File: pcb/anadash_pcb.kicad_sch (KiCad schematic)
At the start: 32 parts, among them J1 Meter1, J2 Meter2, J3 Meter3, J4 Meter4, SW1 SW_Push, SW2 SW_Push, SW3 SW_Push, SW4 SW_Push, SW5 RotaryEncoder_Switch, SW6 SW_Push, SW7 SW_Push, SW8 SW_Push, SW9 SW_Push, U2 ER_OLEDM0.91_1x-I2C

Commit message: pcb design
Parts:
- removed R5, R6, R7, R8: 330, Resistor_THT:R_Axial_DIN0207_L6.3mm_D2.5mm_P7.62mm_Horizontal, symbol Resistors:Resistor - 1%
- R4: renamed from R1; value 330 -> 680
- R5: renamed from R2; value 330 -> 680
- R6: renamed from R3; value 330 -> 680
- R7: renamed from R4; value 330 -> 680
- TP1: value GND -> GNDTP
- TP2: value 5VTestPoint -> 5VTP
- TP3: value 3V3TestPoint -> 3V3TP
- U2: footprint Display:ER_OLEDM0.91_1x-I2C -> Display:Adafruit_SSD1306
- renumbered R10 to R1, R11 to R2, R9 to R3
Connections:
- net +3V3: now also U1.7 (VCC); no longer U1. (VCC)
- net GND: now also U1.8 (GND); no longer U1. (VCC)
- net SCL: now also U1.9 (SCL); no longer U1. (VCC)
- net SDA: now also U1.10 (SDA); no longer U1. (VCC)
- net at J2.1 (Pin_1): now also R5.2
- net at R6.2: now also J3.1 (Pin_1)
- net at R5.1: now also U1.3 (VB); no longer U1. (VCC)
- net at R4.1: now also U1.2 (VA); no longer U1. (VCC)
- net at R7.1: now also U1.5 (VD); no longer U1. (VCC)
- net at R6.1: now also U1.4 (VC); no longer U1. (VCC)
- net at J4.1 (Pin_1): now also R7.2
- net at J1.1 (Pin_1): now also R4.2
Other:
- moved on the sheet: J1, J2, J3, J4

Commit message: fresh start to pcb
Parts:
- U2: footprint Display:Adafruit_SSD1306 -> Connector_JST:JST_XH_B4B-XH-A_1x04_P2.50mm_Vertical
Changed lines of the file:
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@@
 			)
 		)
-		(property "Footprint" "Display:Adafruit_SSD1306"
+		(property "Footprint" "Connector_JST:JST_XH_B4B-XH-A_1x04_P2.50mm_Vertical"
 			(at 247.904 110.49 0)
 			(hide yes)

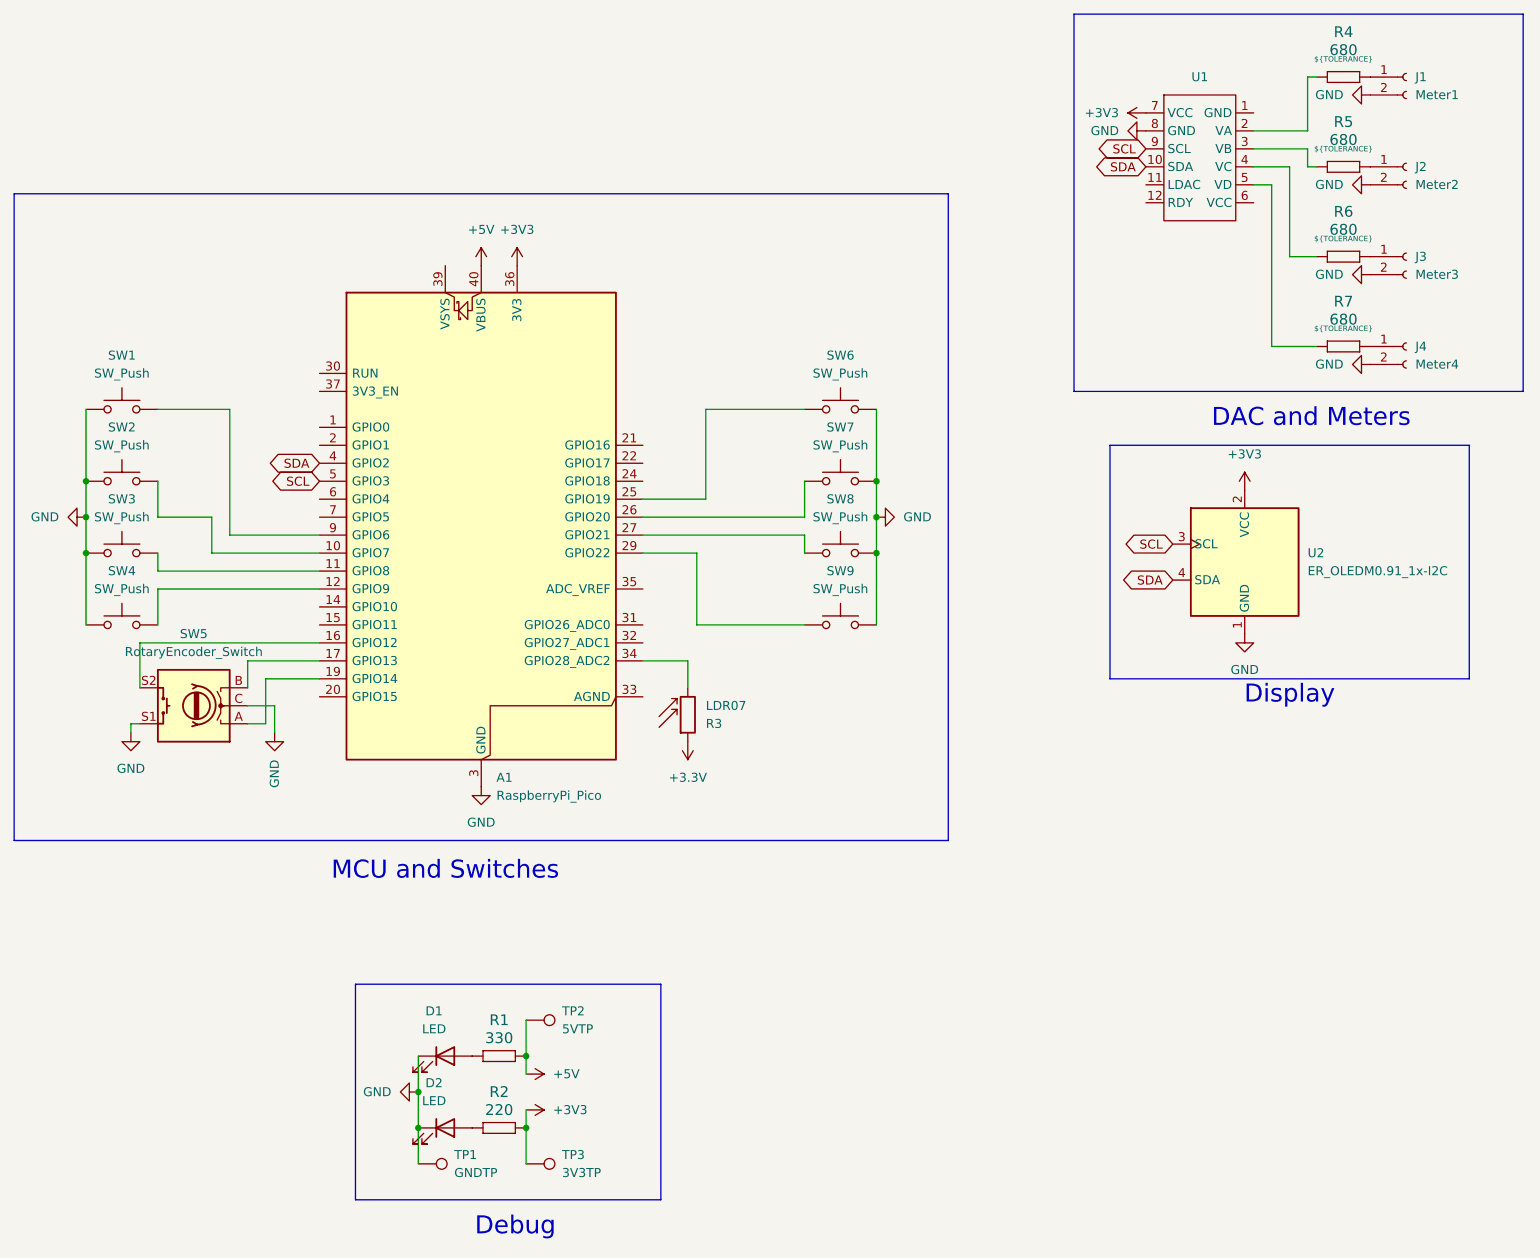
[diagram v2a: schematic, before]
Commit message: Make the schematics pretty, no PCB tho
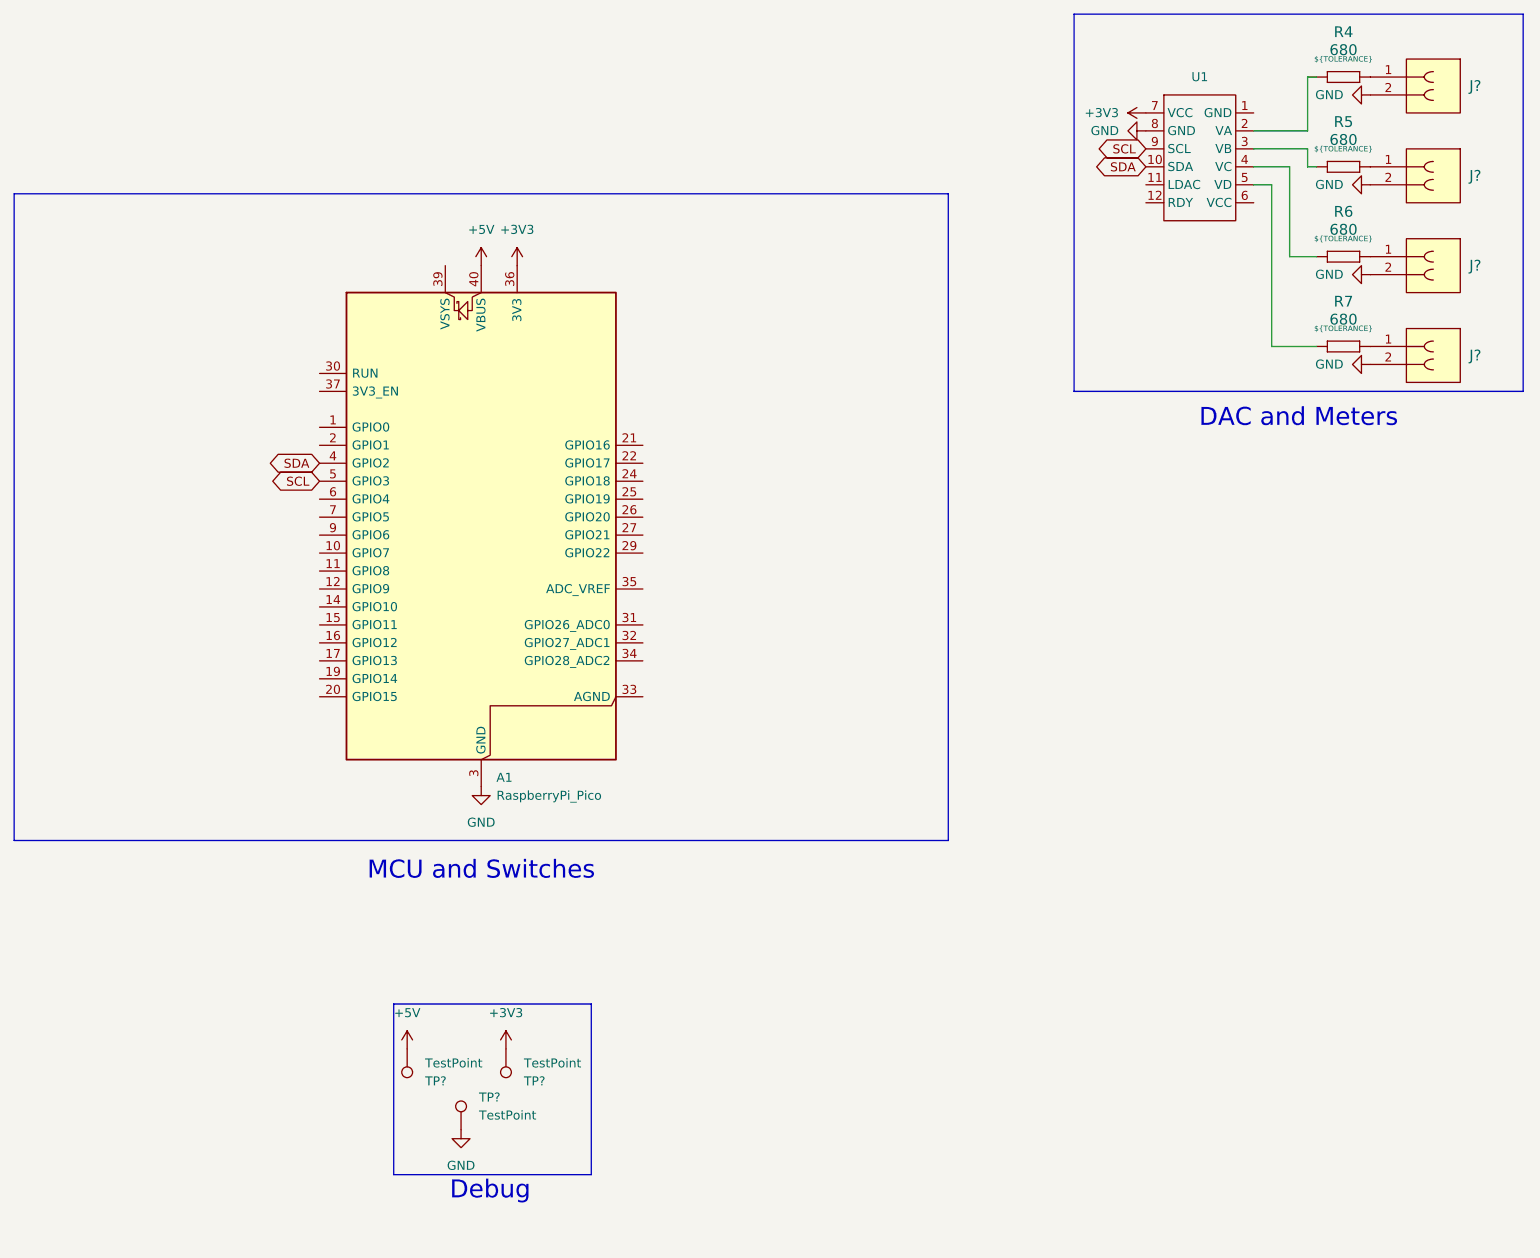
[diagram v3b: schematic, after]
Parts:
- removed D1, D2: LED, LED_THT:LED_D5.0mm, symbol Device:LED
- removed J1: Meter1, Connector_JST:JST_XH_B2B-XH-A_1x02_P2.50mm_Vertical, symbol Connector:Conn_01x02_Socket
- removed J2: Meter2, Connector_JST:JST_XH_B2B-XH-A_1x02_P2.50mm_Vertical, symbol Connector:Conn_01x02_Socket
- removed J3: Meter3, Connector_JST:JST_XH_B2B-XH-A_1x02_P2.50mm_Vertical, symbol Connector:Conn_01x02_Socket
- removed J4: Meter4, Connector_JST:JST_XH_B2B-XH-A_1x02_P2.50mm_Vertical, symbol Connector:Conn_01x02_Socket
- removed R1: 330, Resistor_THT:R_Axial_DIN0207_L6.3mm_D2.5mm_P7.62mm_Horizontal, symbol Resistors:Resistor
- removed R2: 220, Resistor_THT:R_Axial_DIN0207_L6.3mm_D2.5mm_P7.62mm_Horizontal, symbol Resistors:Resistor
- removed R3: LDR07, OptoDevice:R_LDR_5.1x4.3mm_P3.4mm_Vertical, symbol Sensor_Optical:LDR07
- removed SW1, SW2, SW3, SW4, SW6, SW7, SW8, SW9: SW_Push, Button_Switch_Keyboard:SW_Cherry_MX_1.00u_PCB, symbol Switch:SW_Push
- removed SW5: RotaryEncoder_Switch, Rotary_Encoder:RotaryEncoder_Alps_EC11E-Switch_Vertical_H20mm, symbol Device:RotaryEncoder_Switch
- removed TP1: GNDTP, TestPoint:TestPoint_Pad_D2.0mm, symbol Connector:TestPoint
- removed TP2: 5VTP, TestPoint:TestPoint_Pad_D2.0mm, symbol Connector:TestPoint
- removed TP3: 3V3TP, TestPoint:TestPoint_Pad_D2.0mm, symbol Connector:TestPoint
- removed U2: ER_OLEDM0.91_1x-I2C, Connector_JST:JST_XH_B4B-XH-A_1x04_P2.50mm_Vertical, symbol Display_Graphic:ER_OLEDM0.91_1x-I2C
- added J? (x4): ${FAMILY}, symbol Connectors:Connector 2 Female
- added TP? (x3): TestPoint, symbol Connector:TestPoint
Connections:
- net +3V3: now also TP?.1
- net +5V: now also TP?.1
- net GND: now also J?.2, J?.2, J?.2, J?.2, TP?.1
- net at R5.2: now also J?.1
- net at R6.2: now also J?.1
- net at R7.2: now also J?.1
- net at R4.2: now also J?.1
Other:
- note removed: "Display"

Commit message: Finish the schematic ig
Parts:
- added J1, J4: ${FAMILY}, symbol Connectors:Connector 4 Female
- added J2, J3: ${FAMILY}, symbol Connectors:Connector 5 Female
- gave numbers to parts that had none: 7
- renumbered R4 to R1, R5 to R2, R6 to R3, R7 to R4
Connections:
- net +3V3: now also J1.2
- net GND: now also J1.1, J2.3, J3.3, J4.2
- net SCL: now also J1.4
- net SDA: now also J1.3
- net at A1.10 (GPIO7): now also J2.5
- net at A1.11 (GPIO8): now also J3.1
- net at A1.12 (GPIO9): now also J3.2
- net at A1.14 (GPIO10): now also J3.4
- net at A1.15 (GPIO11): now also J3.5
- net at A1.16 (GPIO12): now also J4.1
- net at A1.17 (GPIO13): now also J4.3
- net at A1.19 (GPIO14): now also J4.4
- net at A1.6 (GPIO4): now also J2.1
- net at A1.7 (GPIO5): now also J2.2
- net at A1.9 (GPIO6): now also J2.4
